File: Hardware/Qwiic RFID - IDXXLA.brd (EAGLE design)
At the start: 25.4 x 30.5 mm, 60 parts, among them J3 PTH, J8 AVR_SPI_PROG_3X2TESTPOINTS, Q1 600mA/40V, U1 ATTINY84-ARDUINO, U2 ID-12/20SMD

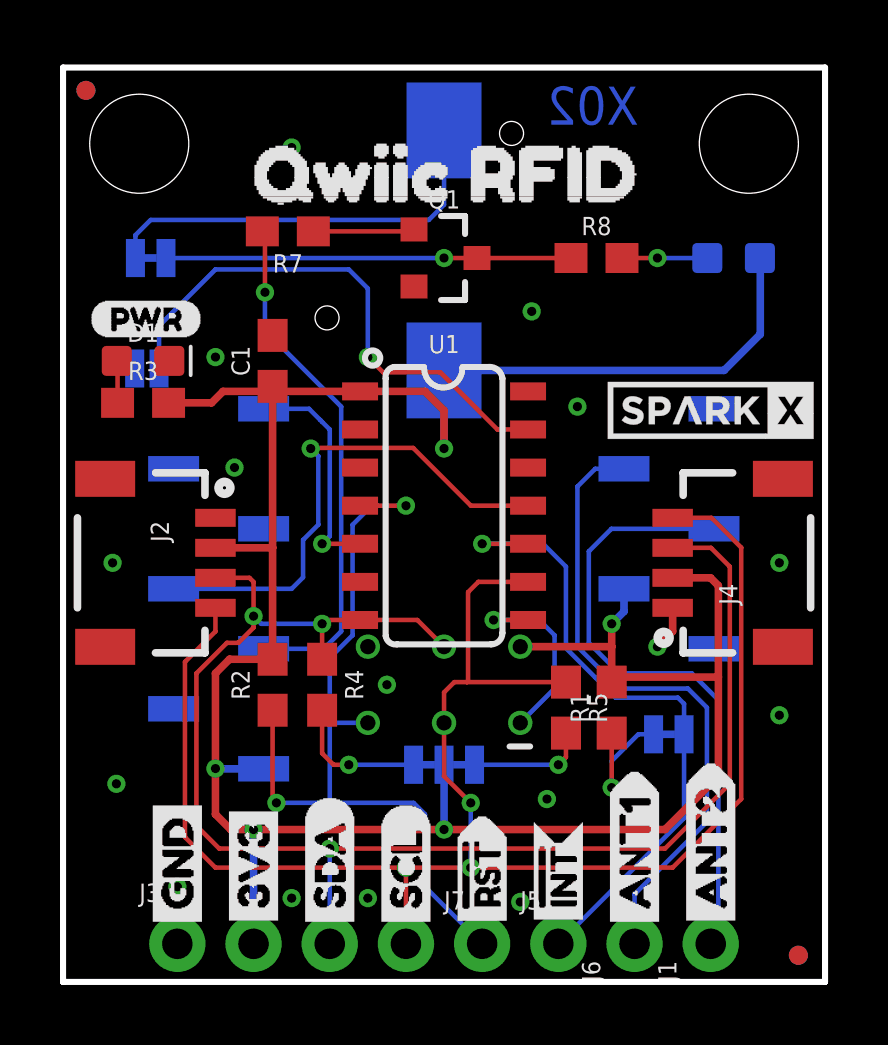
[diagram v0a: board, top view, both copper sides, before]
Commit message: Updates general trace layout, moves interrupt jumper to upper right, moves stat LED to TOP layer parallel with PWR LED
* Adds SparkFun Flame and removes SparkX references
* Changes version
* Updates text to vector in schematic.
* Updates Qwiic_RFID silk and power LED to something larger.
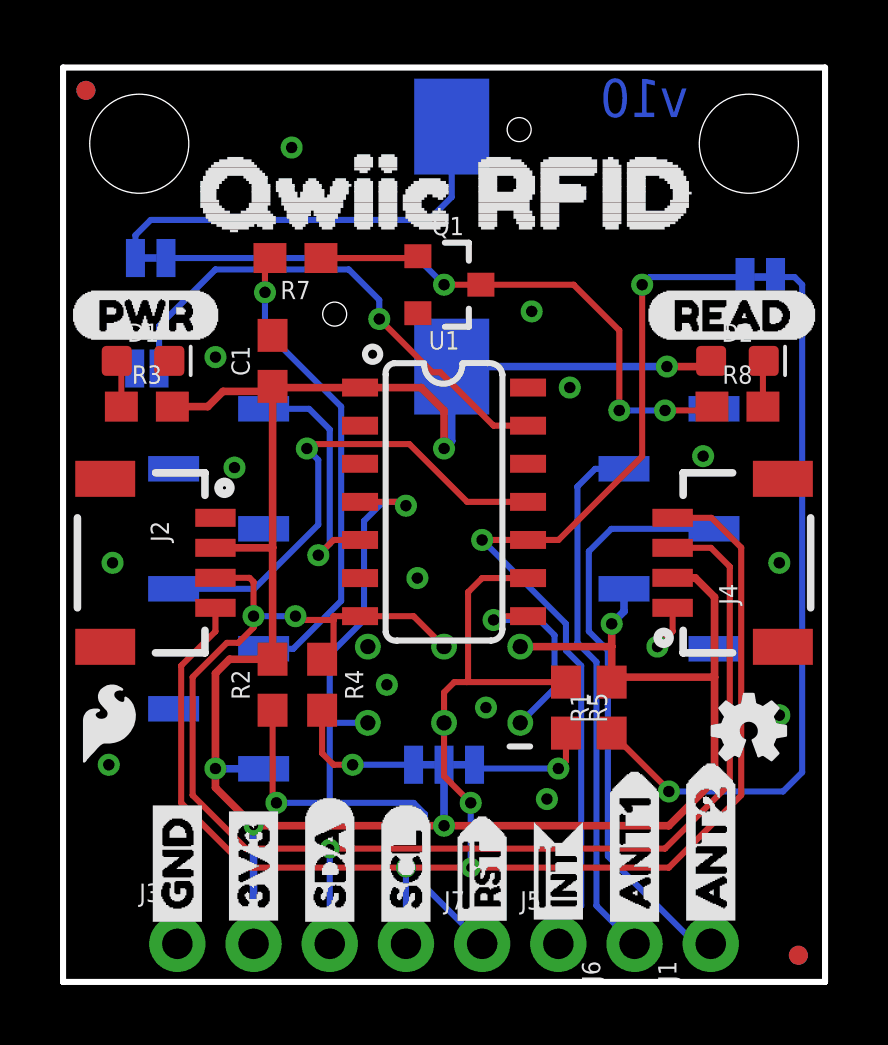
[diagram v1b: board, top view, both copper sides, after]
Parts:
- removed U$14: (no value), Labels:PWR-()-03
- removed U$19: (no value), QWIIC_RFID:QWIIC_RFID0
- added LOGO2: SFE_LOGO_FLAME.1_INCH, SparkFun-Aesthetics:SFE_LOGO_FLAME_.1
- U$1: device SparkX:SPARKX-TINY -> Qwiic_RFID_BIG:QWIIC_RFID0
- U$4: value SPARKX-LOGO3 -> (none); device SparkX:SPARKX-SMALL -> Labels:PWR-()-04
- moved U$4 21.6 mm to (0.25, 22.2)
- moved LOGO1 20.6 mm to (22.9, 8.38), flipped to the top
- moved U$13 19.8 mm to (24.8, 25.4), turned to 0 degrees
- moved JP8 15.5 mm to (23.2, 23.5), turned to 180 degrees
- moved R8 6.83 mm to (22.5, 19.2)
- moved U$1 5.97 mm to (2.41, 26.3), flipped to the top
- moved U$18 5.72 mm to (19.4, 22.2), flipped to the top
- moved D2 3.43 mm to (22.5, 20.7), flipped to the top
- moved R7 0.92 mm to (7.75, 24.1)
- moved Q1 0.90 mm to (12.8, 23.2)
- moved LS1 0.28 mm to (13.0, 24.5)
- moved R3 0.18 mm to (2.79, 19.2)
- moved U1 0.13 mm to (12.7, 16.6)
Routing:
- net N$4: track 4.47 -> 24.7 mm
- net !INT: track 21.8 -> 30.9 mm, vias 1 -> 2
- net N$8: track 13.5 -> 21.9 mm, vias 1 -> 3
- net 3.3V: track 88.2 -> 82.3 mm, vias 5 -> 6
- net ANT2: track 21.2 -> 17.8 mm
- net LED_BUZZ: track 17.4 -> 15.8 mm
- net ANT1: track 20.9 -> 19.5 mm
- net N$5: track 2.85 -> 1.54 mm, vias 1 -> 0
- net N$6: track 18.0 -> 17.0 mm
- net TAG_IN_RANGE: track 7.67 -> 8.44 mm
- net SCL/SCK: track 57.2 -> 56.7 mm
- net GND: vias 16 -> 15
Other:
- board text added: "v10"
- board text removed: "X02"

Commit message: Adds better SparkFun silk, changes text to vector, and updates product name silk
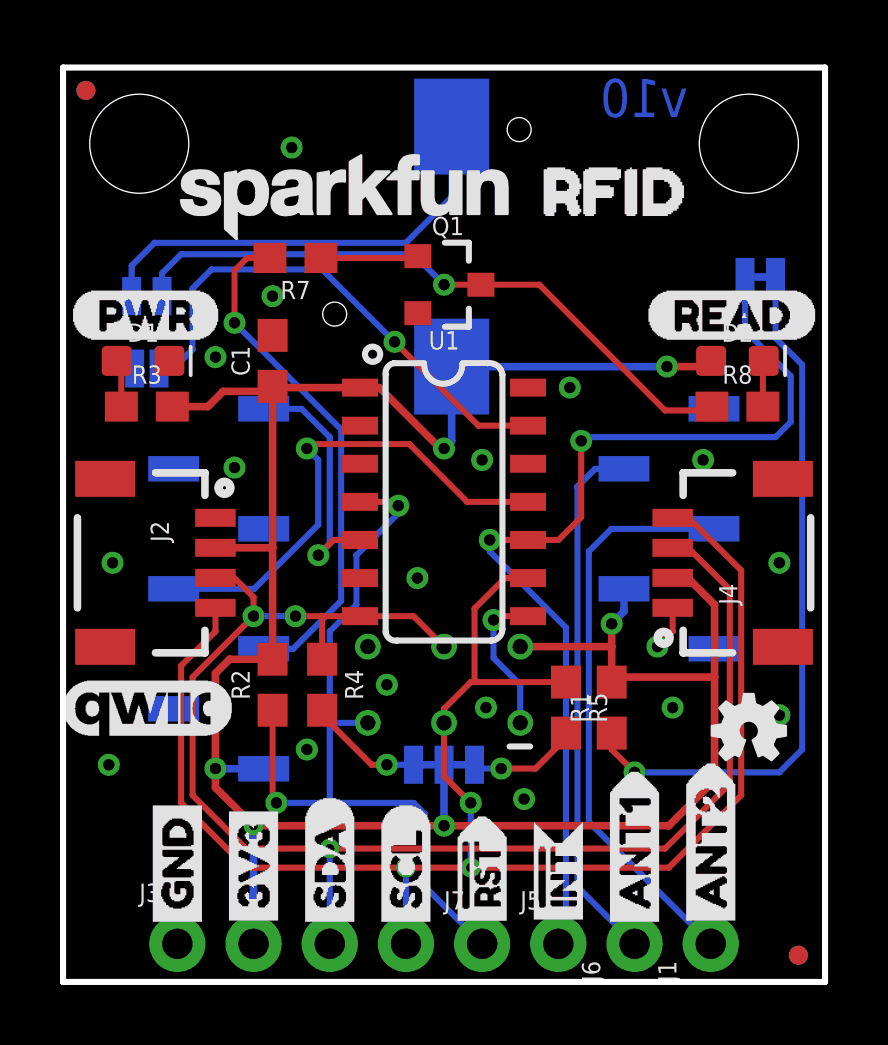
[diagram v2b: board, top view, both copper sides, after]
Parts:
- LOGO2: value SFE_LOGO_FLAME.1_INCH -> SFE_LOGO_NAME.1_INCH; device SparkFun-Aesthetics:SFE_LOGO_FLAME_.1 -> SparkFun-Aesthetics:SFE_LOGO_NAME_.1
- U$1: device Qwiic_RFID_BIG:QWIIC_RFID0 -> Labels:QWIIC_COPYRIGHT_SMALL
- U$8: device Labels:QWIIC-LOGO-MEDIUM -> QWIIC_RFID:RFID0
- moved LOGO2 19.2 mm to (9.40, 26.2)
- moved U$1 17.1 mm to (2.79, 9.14)
- moved U$8 11.4 mm to (14.6, 26.3), flipped to the top
- moved U$15 2.29 mm to (5.71, 24.6)
- moved JP9 1.28 mm to (2.79, 22.9)
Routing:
- net !INT: track 30.9 -> 33.2 mm
- net MISO: track 6.84 -> 5.00 mm
- net SCL/SCK: track 56.7 -> 55.3 mm
- net LED_BUZZ: track 15.8 -> 17.1 mm
- net SDA/MOSI: track 50.0 -> 48.9 mm
- net N$4: track 24.7 -> 23.6 mm
- net !RST: track 27.8 -> 26.8 mm
- net 3.3V: track 82.3 -> 81.4 mm
- net N$9: track 14.2 -> 15.0 mm
- net N$2: track 4.64 -> 3.90 mm
- net N$8: track 21.9 -> 21.6 mm, vias 3 -> 1
- net GND: vias 15 -> 18

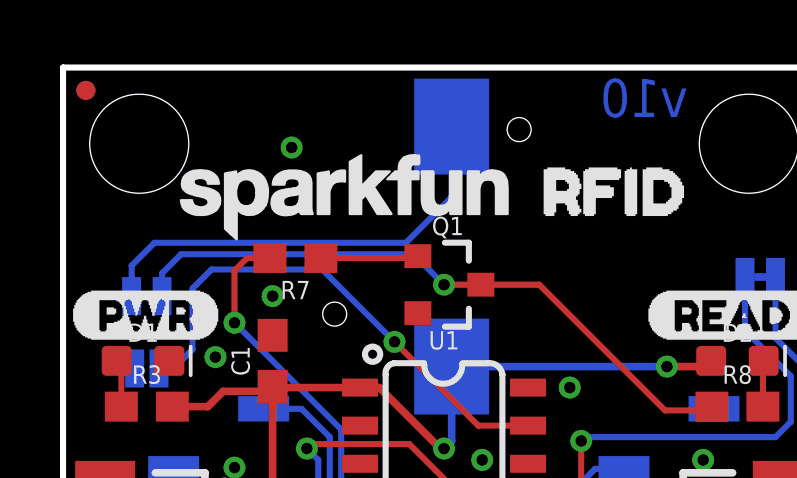
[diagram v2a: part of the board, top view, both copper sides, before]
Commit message: Changes sparkFun logo to sparkFun + flame logo, adds dimensions for standoffs
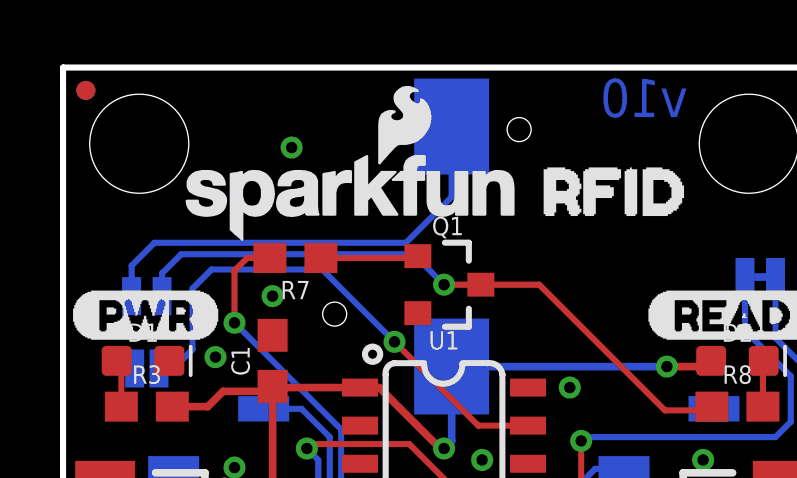
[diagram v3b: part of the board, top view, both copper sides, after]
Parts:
- removed LOGO2: SFE_LOGO_NAME.1_INCH, SparkFun-Aesthetics:SFE_LOGO_NAME_.1
- added LOGO3: SFE_LOGO_NAME_FLAME.1_INCH, SparkFun-Aesthetics:SFE_LOGO_NAME_FLAME_.1
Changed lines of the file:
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@@
 <drawing>
 <settings>
-<setting alwaysvectorfont="yes"/>
+<setting alwaysvectorfont="no"/>
 <setting keepoldvectorfont="yes"/>
 <setting verticaltext="up"/>
 </settings>
-<grid distance="0.01" unitdist="inch" unit="inch" style="lines" multiple="1" display="yes" altdistance="0.001" altunitdist="inch" altunit="inch"/>
+<grid distance="0.05" unitdist="inch" unit="inch" style="lines" multiple="1" display="yes" altdistance="0.005" altunitdist="inch" altunit="inch"/>
 <layers>
 <layer number="1" name="Top" color="4" fill="1" visible="yes" active="yes"/>
@@
 <layer number="37" name="tTest" color="7" fill="1" visible="no" active="yes"/>
 <layer number="38" name="bTest" color="7" fill="1" visible="no" active="yes"/>
-<layer number="39" name="tKeepout" color="4" fill="11" visible="yes" active="yes"/>
+<layer number="39" name="tKeepout" color="4" fill="11" visible="no" active="yes"/>
 <layer number="40" name="bKeepout" color="1" fill="11" visible="no" active="yes"/>
 <layer number="41" name="tRestrict" color="4" fill="10" visible="no" active="yes"/>
@@
 <layer number="45" name="Holes" color="7" fill="1" visible="yes" active="yes"/>
 <layer number="46" name="Milling" color="3" fill="1" visible="no" active="yes"/>
-<layer number="47" name="Measures" color="7" fill="1" visible="no" active="yes"/>
+<layer number="47" name="Measures" color="7" fill="1" visible="yes" active="yes"/>
 <layer number="48" name="Document" color="7" fill="1" visible="no" active="yes"/>
 <layer number="49" name="Reference" color="13" fill="1" visible="yes" active="yes"/>
@@
 <layer number="115" name="ReferenceISLANDS" color="7" fill="1" visible="no" active="no"/>
 <layer number="116" name="Patch_BOT" color="9" fill="4" visible="no" active="no"/>
-<layer number="117" name="PM_Ref" color="26" fill="1" visible="no" active="yes"/>
+<layer number="117" name="PM_Ref" color="26" fill="1" visible="yes" active="yes"/>
 <layer number="118" name="Rect_Pads" color="7" fill="1" visible="no" active="no"/>
-<layer number="119" name="PF_Ref" color="31" fill="1" visible="no" active="yes"/>
+<layer number="119" name="PF_Ref" color="31" fill="1" visible="yes" active="yes"/>
 <layer number="120" name="WFL_Ref" color="25" fill="1" visible="yes" active="yes"/>
 <layer number="121" name="_tsilk" color="7" fill="1" visible="no" active="no"/>
@@
 <dimension x1="25.4" y1="30.48" x2="0" y2="30.48" x3="12.7" y3="34.29" textsize="1.778" textratio="15" layer="47" unit="inch"/>
 <text x="20.828" y="28.829" size="1.27" layer="16" font="vector" ratio="15" rot="MR0">v10</text>
+<dimension x1="2.54" y1="27.94" x2="2.54" y2="30.48" x3="-1.27" y3="29.21" textsize="1.778" textratio="15" layer="47" unit="inch"/>
+<dimension x1="22.86" y1="27.94" x2="25.4" y2="27.94" x3="24.13" y3="33.02" textsize="1.778" textratio="15" layer="47" unit="inch"/>
 </plain>
 <attributes>
@@
 <element name="U$4" library="Labels" package="PWR-()-04" value="" x="0.254" y="22.225" smashed="yes"/>
 <element name="U$1" library="Labels" package="QWIIC_COPYRIGHT_SMALL" value="" x="2.794" y="9.144" smashed="yes"/>
-<element name="LOGO2" library="SparkFun-Aesthetics" package="SFE_LOGO_NAME_.1" value="SFE_LOGO_NAME.1_INCH" x="9.398" y="26.162" smashed="yes"/>
 <element name="U$8" library="QWIIC_RFID" package="RFID0" value="" x="14.5796" y="26.3398" smashed="yes"/>
+<element name="LOGO3" library="SparkFun-Aesthetics" package="SFE_LOGO_NAME_FLAME_.1" value="SFE_LOGO_NAME_FLAME.1_INCH" x="9.652" y="26.162" smashed="yes"/>
 </elements>
 <signals>
